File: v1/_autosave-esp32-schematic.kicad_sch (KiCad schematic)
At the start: 46 parts, among them J1 GN-2630G, J10 Screw_Terminal_01x04, J11 Screw_Terminal_01x04, J12 Screw_Terminal_01x04, J13 Screw_Terminal_01x04, J15 POWER, J2 Jumper, J3 Micro_SD_Card, J4 Screw_Terminal_01x04, J5 Screw_Terminal_01x04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

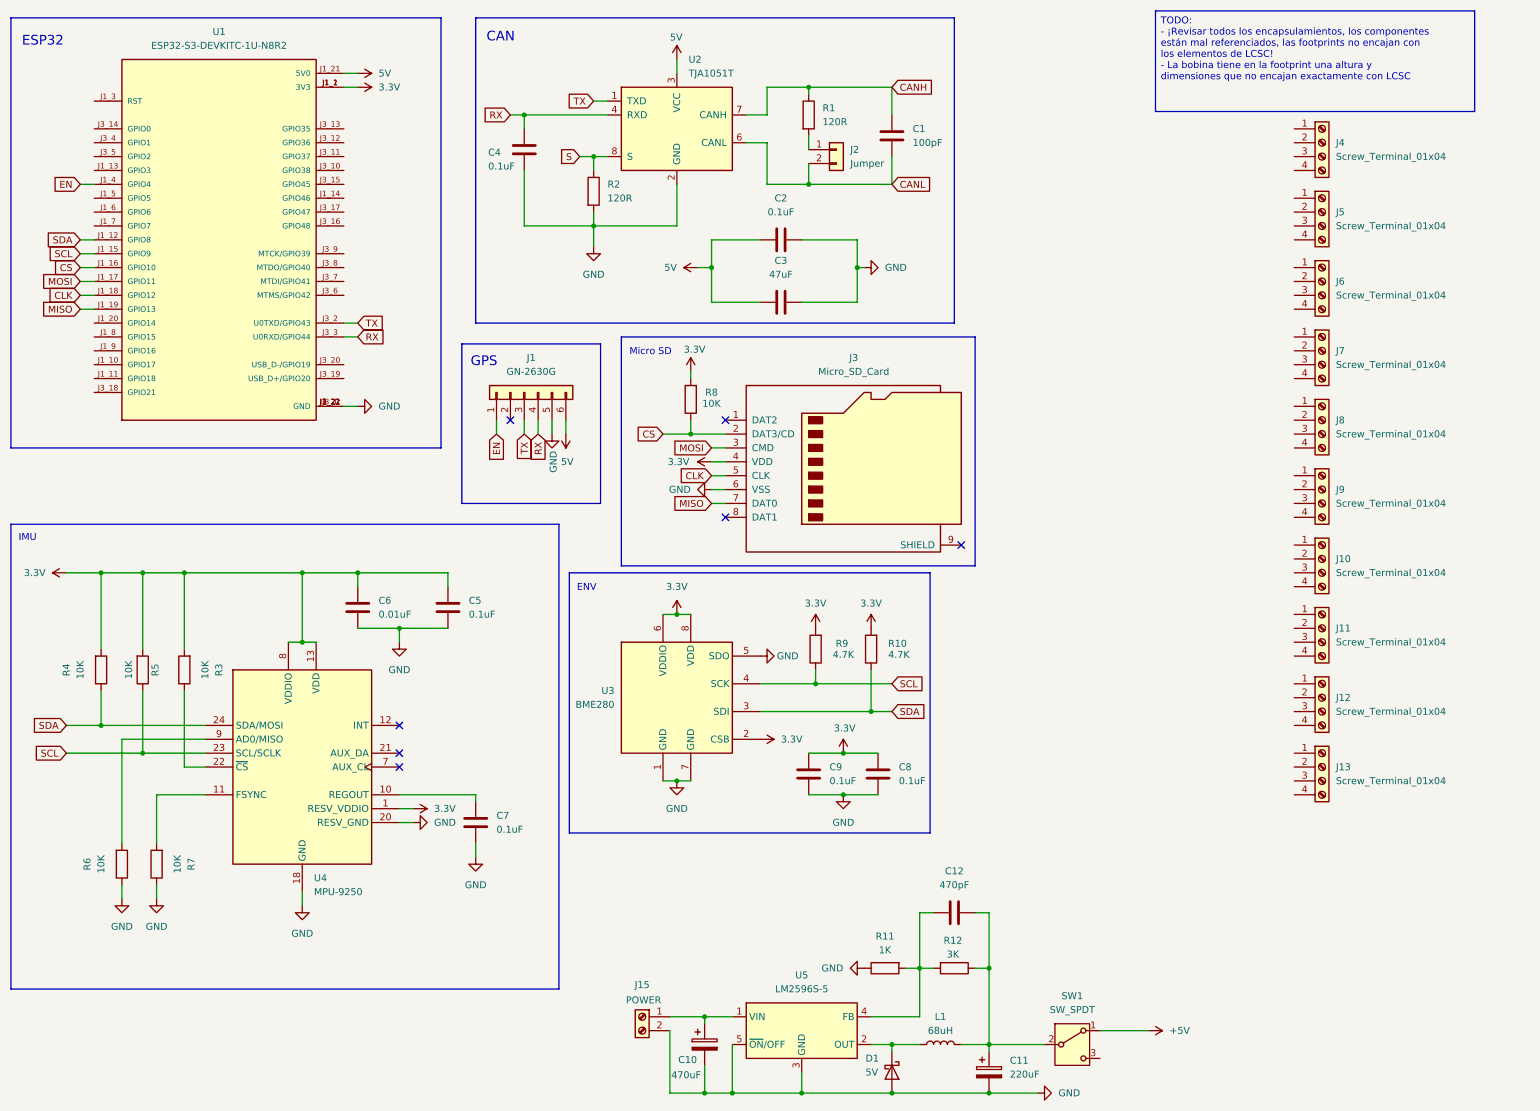
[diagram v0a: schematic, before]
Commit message: Reorganisation of the project, the v1 will be the test prototype and the v2 will be implementing the devices on the board directly. Also the libraries have been reorganised, each version will share all the libraries, this way we can stop importing the same components over and over. Also a recommended command to add to the source in case you are using linux, see the README
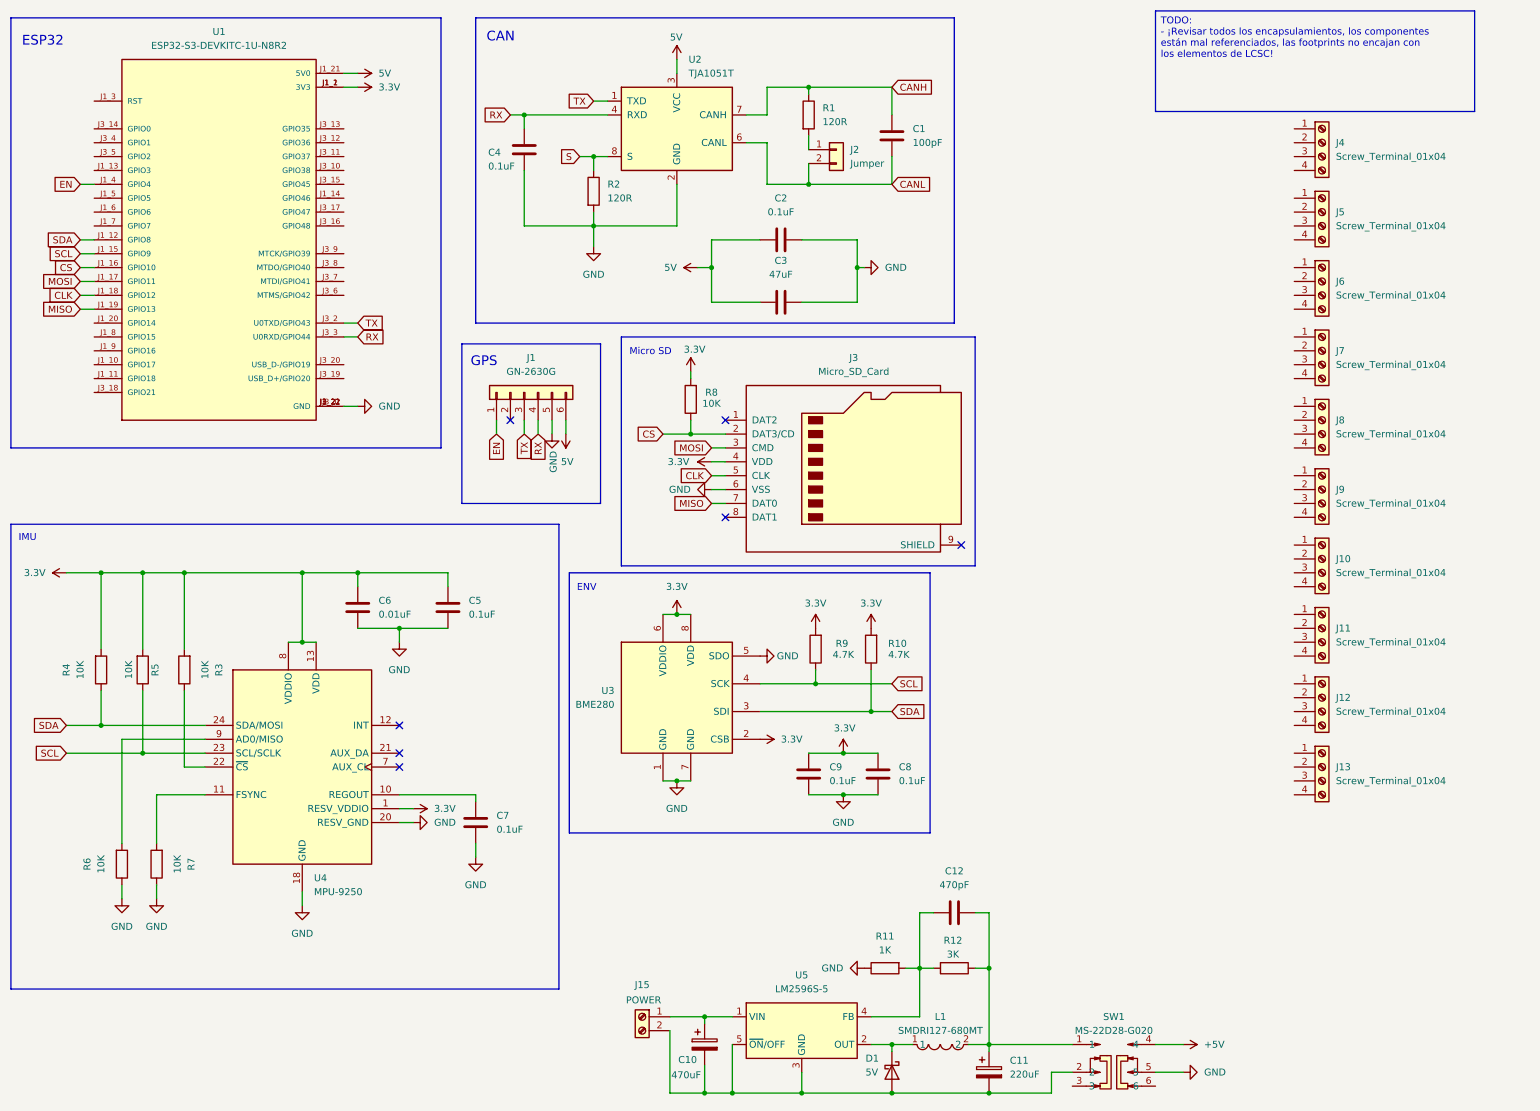
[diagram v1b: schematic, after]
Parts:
- removed L1: 68uH, Inductor_SMD:L_12x12mm_H6mm, symbol Device:L
- removed SW1: SW_SPDT, Button_Switch_SMD:SW_DPDT_CK_JS202011JCQN, symbol Switch:SW_SPDT
- added L1: SMDRI127-680MT, easyeda2kicad:IND-SMD_L12.3-W12.3_SMDRI127, symbol easyeda2kicad:SMDRI127-680MT
- added SW1: MS-22D28-G020, easyeda2kicad:SW-SMD_MS-22D28-G020, symbol easyeda2kicad:MS-22D28-G020
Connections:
- net +5V: now also SW1.4
- net GND: now also SW1.5; no longer C10.2, C11.2, D1.2 (A), J15.2 (Pin_2), U5.3 (GND), U5.5 (~{ON}/OFF)
- net at D1.1 (K), U5.2 (OUT): now also L1.1
- net at C11.1, C12.2, R12.1: now also L1.2, SW1.1
- new net: C10.2, C11.2, D1.2 (A), J15.2 (Pin_2), SW1.2, U5.3 (GND), U5.5 (~{ON}/OFF)
